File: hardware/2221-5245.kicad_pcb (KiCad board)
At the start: 2 copper layers, 35 x 11.9 mm, 11 parts, among them J1 USB-micro-B-8192, U1 MCP2221AxSL, U2 AD5245

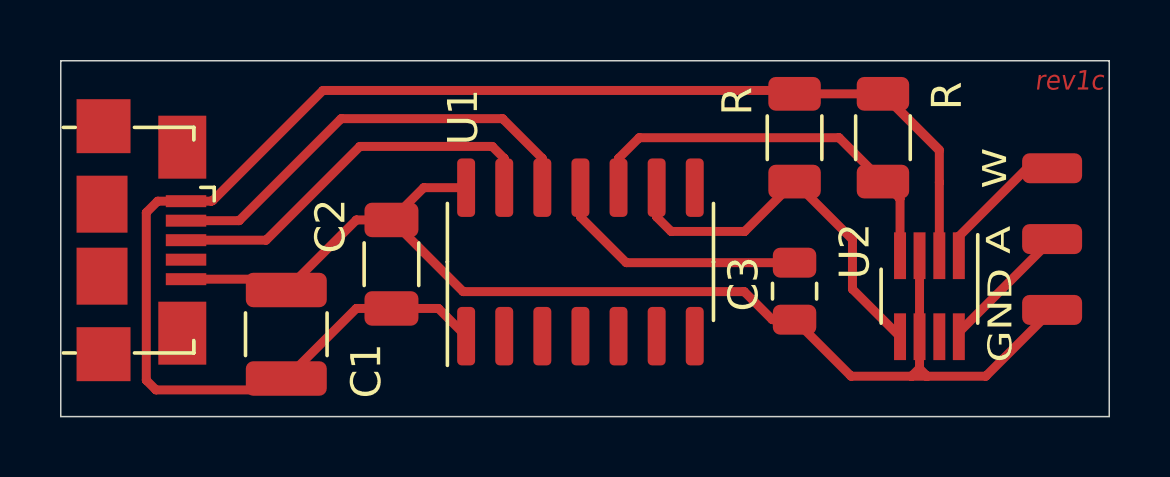
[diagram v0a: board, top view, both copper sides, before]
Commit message: Update footprints in kicad pcb file
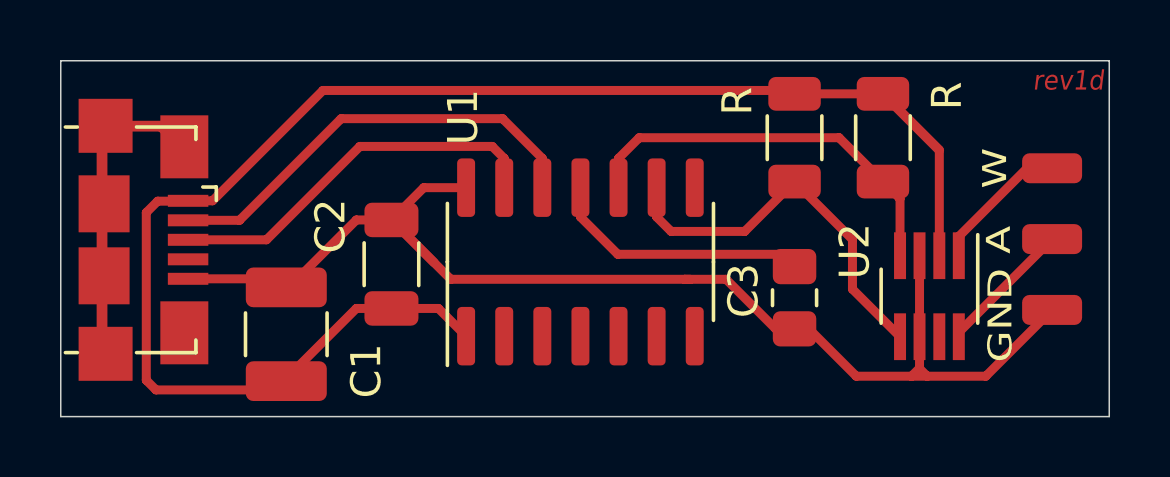
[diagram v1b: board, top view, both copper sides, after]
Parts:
- C1: footprint Capacitor_SMD:C_1210_3225Metric -> Capacitor_SMD:C_1210_3225Metric_Pad1.33x2.70mm_HandSolder
- C3: footprint Capacitor_SMD:C_0805_2012Metric -> Capacitor_SMD:C_0805_2012Metric_Pad1.18x1.45mm_HandSolder
- moved C3 0.22 mm to (60.8, 43.7)
- moved J1 0.07 mm to (39.2, 41.7)
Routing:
- net Net-(J1-Pad6): track 0.00 -> 10.6 mm
- net GND: track 41.0 -> 43.6 mm
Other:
- board text added: "Single-sided version 1b - first batch to be fabricated 1c - fixed solder mask on USB connector 1d - increased cap footprints, small changes to usb connector"
- board text added: "rev1d"
- board text removed: "Single-sided version 1a - prototype 1b - first batch that was fabricated 1c - fixed solder mask on USB connector"
- board text removed: "rev1c"
